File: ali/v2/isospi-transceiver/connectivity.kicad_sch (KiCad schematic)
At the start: 27 parts, among them J7 Conn_01x03, J8 Vertical Ethernet, U3 TJA1462ATK, U4 LAN8742AI, Y2 25 MHz

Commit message: Some BoM Changes, add fabrication toolkit settings
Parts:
- R10, R11, R12, R13: MPN RC0603FR-0747RL -> AC0603FR-0747RL
- R14, R16: MPN RC0603FR-0710KL -> AC0603FR-0710KL
- R17, R18: MPN RC0603FR-07330RL -> AC0603FR-07330RL
- R9: MPN RC0603FR-071K5L -> AC0603FR-071K5L
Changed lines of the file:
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@@
 			)
 		)
-		(property "MPN" "RC0603FR-0747RL"
+		(property "MPN" "AC0603FR-0747RL"
 			(at 100.33 68.58 0)
 			(hide yes)
@@
 			)
 		)
-		(property "MPN" "RC0603FR-0710KL"
+		(property "MPN" "AC0603FR-0710KL"
 			(at 53.34 85.09 90)
 			(hide yes)
@@
 			)
 		)
-		(property "MPN" "RC0603FR-0747RL"
+		(property "MPN" "AC0603FR-0747RL"
 			(at 134.62 68.58 0)
 			(hide yes)
@@
 			)
 		)
-		(property "MPN" "RC0603FR-0747RL"
+		(property "MPN" "AC0603FR-0747RL"
 			(at 111.76 68.58 0)
 			(hide yes)
@@
 			)
 		)
-		(property "MPN" "RC0603FR-07330RL"
+		(property "MPN" "AC0603FR-07330RL"
 			(at 229.87 120.65 0)
 			(hide yes)
@@
 			)
 		)
-		(property "MPN" "RC0603FR-0710KL"
+		(property "MPN" "AC0603FR-0710KL"
 			(at 99.06 102.87 0)
 			(hide yes)
@@
 			)
 		)
-		(property "MPN" "RC0603FR-071K5L"
+		(property "MPN" "AC0603FR-071K5L"
 			(at 43.18 67.31 0)
 			(hide yes)
@@
 			)
 		)
-		(property "MPN" "RC0603FR-07330RL"
+		(property "MPN" "AC0603FR-07330RL"
 			(at 220.98 130.81 0)
 			(hide yes)
@@
 			)
 		)
-		(property "MPN" "RC0603FR-0747RL"
+		(property "MPN" "AC0603FR-0747RL"
 			(at 123.19 68.58 0)
 			(hide yes)

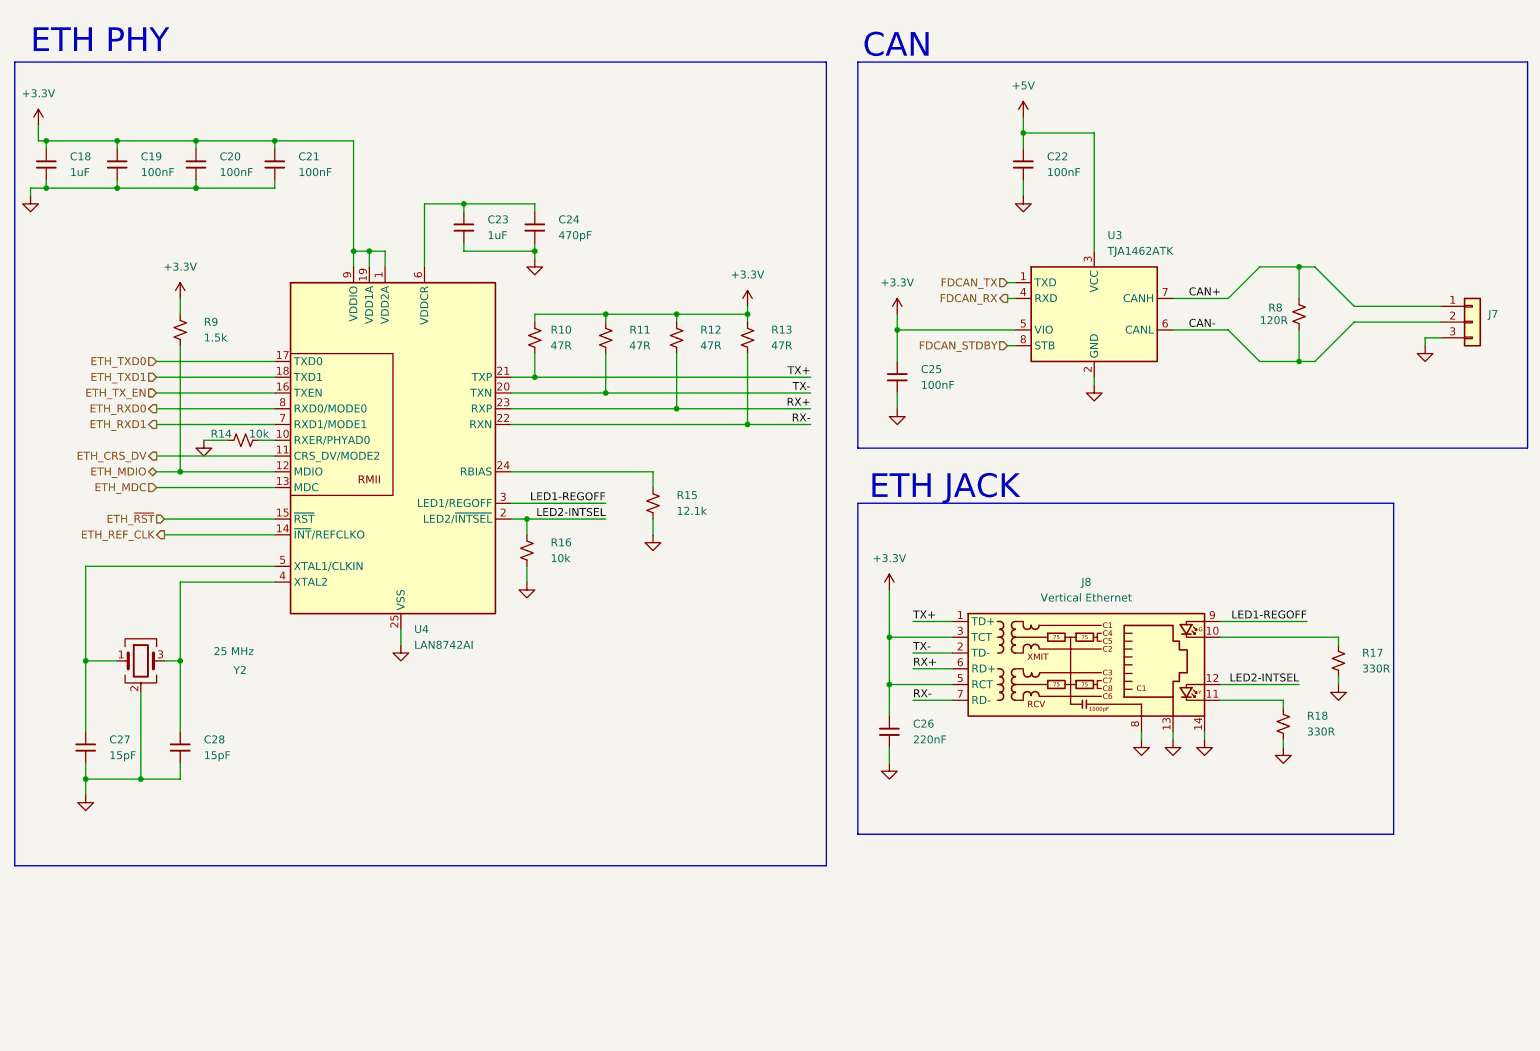
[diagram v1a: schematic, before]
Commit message: Use 1206 on AFEs
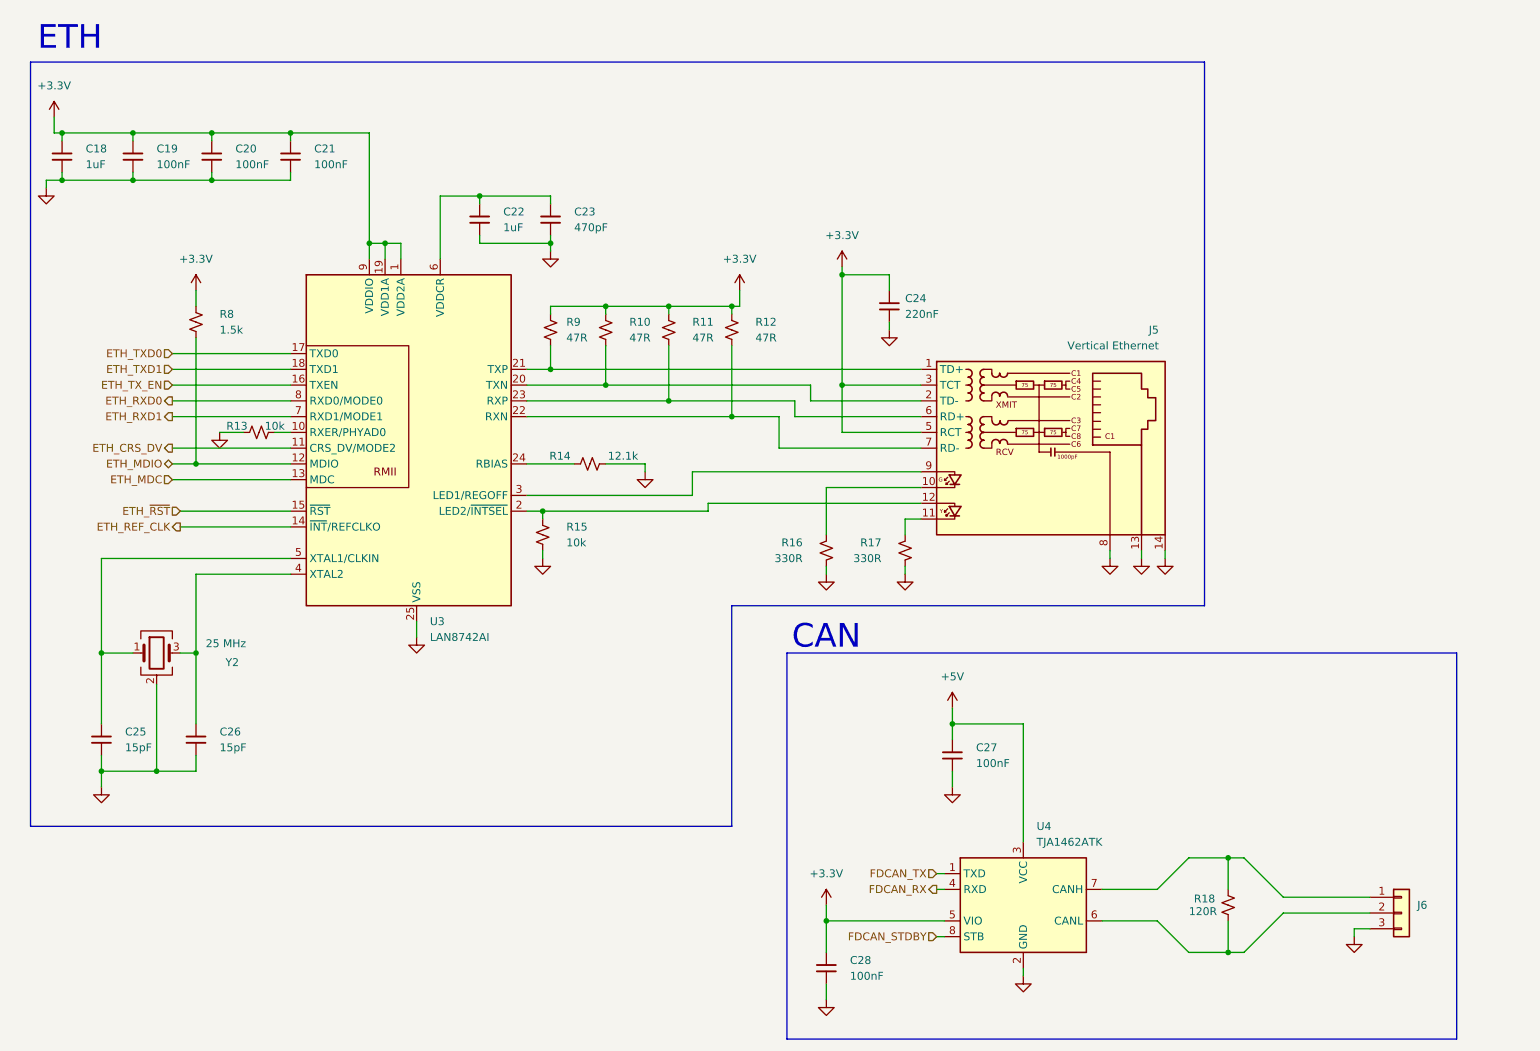
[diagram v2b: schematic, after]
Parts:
- removed J7: Conn_01x03, APRL_Connector_Molex:Molex_CLIK-Mate_503159-0301_1x03-1MP_P1.50mm_Vertical, symbol Connector_Generic:Conn_01x03
- removed J8: Vertical Ethernet, APRL_Connector:RJ45_Hanrun_HY951180A_Vertical, symbol APRL_Connector:RJ45_Hanrun_HY951180A
- removed U3: TJA1462ATK, APRL_Package_QFN:HVSON-8-1EP_3x3mm_P0.65mm_EP1.6x2.4mm_ThermalVias, symbol APRL_Comms:TJA1462ATK
- removed U4: LAN8742AI, APRL_Package_QFN:VQFN-24-1EP_4x4mm_P0.5mm_EP2.5x2.5mm_ThermalVias, symbol APRL_Comms:LAN8742A
- added J5: Vertical Ethernet, APRL_Connector:RJ45_Hanrun_HY951180A_Vertical, symbol APRL_Connector:RJ45_Hanrun_HY951180A
- added J6: Conn_01x03, APRL_Connector_Molex:Molex_CLIK-Mate_503159-0301_1x03-1MP_P1.50mm_Vertical, symbol Connector_Generic:Conn_01x03
- added U3: LAN8742AI, APRL_Package_QFN:VQFN-24-1EP_4x4mm_P0.5mm_EP2.5x2.5mm_ThermalVias, symbol APRL_Comms:LAN8742A
- added U4: TJA1462ATK, APRL_Package_QFN:HVSON-8-1EP_3x3mm_P0.65mm_EP1.6x2.4mm_ThermalVias, symbol APRL_Comms:TJA1462ATK
- C22: value 100nF -> 1uF; MPN GRM188R72A104KA35 -> GRM188D72A105KE01
- C23: value 1uF -> 470pF; MPN GRM188D72A105KE01 -> GRM1885C1H471JA01
- C24: value 470pF -> 220nF; MPN GRM1885C1H471JA01 -> GRM188R71H224KAC4
- C25: value 100nF -> 15pF; MPN GRM188R72A104KA35 -> GRM1885C2E150FW07
- C26: value 220nF -> 15pF; MPN GRM188R71H224KAC4 -> GRM1885C2E150FW07
- C27, C28: value 15pF -> 100nF; MPN GRM1885C2E150FW07 -> GRM188R72A104KA35
- R13: value 47R -> 10k; MPN AC0603FR-0747RL -> AC0603FR-0710KL
- R14: value 10k -> 12.1k; MPN AC0603FR-0710KL -> RT0603BRD0712K1L
- R15: value 12.1k -> 10k; MPN RT0603BRD0712K1L -> AC0603FR-0710KL
- R16: value 10k -> 330R; MPN AC0603FR-0710KL -> AC0603FR-07330RL
- R18: value 330R -> 120R; MPN AC0603FR-07330RL -> AC0603FR-07120RL
- R8: value 120R -> 1.5k; MPN AC0603FR-07120RL -> AC0603FR-071K5L
- R9: value 1.5k -> 47R; MPN AC0603FR-071K5L -> AC0603FR-0747RL
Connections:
- net CAN+ is gone; now on net ETH_MDIO: R8.2
- net CAN- is gone; now on net +3.3V: R8.1
- net +3.3V: now also C24.1, C28.1, J5.3 (TCT), J5.5 (RCT), U3.1 (VDD2A), U3.19 (VDD1A), U3.9 (VDDIO), U4.5 (VIO); no longer C25.1, C26.1, R13.1
- net +5V: now also C27.1, U4.3 (VCC); no longer C22.1
- net ETH_CRS_DV: now also U3.11 (CRS_DV/MODE2)
- net ETH_MDC: now also U3.13 (MDC)
- net ETH_MDIO: now also U3.12 (MDIO); no longer R9.2
- net ETH_REF_CLK: now also U3.14 (~{INT}/REFCLKO)
- net ETH_RXD0: now also U3.8 (RXD0/MODE0)
- net ETH_RXD1: now also U3.7 (RXD1/MODE1)
- net ETH_TXD0: now also U3.17 (TXD0)
- net ETH_TXD1: now also U3.18 (TXD1)
- net ETH_TX_EN: now also U3.16 (TXEN)
- net ETH_~{RST}: now also U3.15 (~{RST})
- net FDCAN_RX: now also U4.4 (RXD)
- net FDCAN_STDBY: now also U4.8 (STB)
- net FDCAN_TX: now also U4.1 (TXD)
- net GND: now also R13.1, R14.2, J5.13, J5.14, J5.8, J6.3 (Pin_3), U3.25 (VSS), U4.2 (GND), U4.9 (GND); no longer R14.1, R18.2
- net at Y2.1: now also C25.1, U3.5 (XTAL1/CLKIN); no longer C27.1
- net at C23.1: now also C22.1, U3.6 (VDDCR); no longer C24.1
- net at R17.1: now also J5.11
- net at R18.1: now also J6.2 (Pin_2), U4.6 (CANL)
- net at R15.1: now also J5.12, U3.2 (LED2/~{INTSEL})
- net at Y2.3: now also C26.1, U3.4 (XTAL2); no longer C28.1
- net LED2-INTSEL: no longer names the net of R16.1
- net LED2-INTSEL: now also J5.10
- net RX+: no longer names the net of R12.2
- net RX+: now also J5.7 (RD-), U3.22 (RXN)
- net RX-: no longer names the net of R13.2
- net RX-: now also U3.10 (RXER/PHYAD0)
- net TX+: no longer names the net of R10.2
- net TX+: now also J5.2 (TD-), U3.20 (TXN)
- net TX-: no longer names the net of R11.2
- net TX-: now also J5.6 (RD+), U3.23 (RXP)
- new net: J6.1 (Pin_1), R18.2, U4.7 (CANH)
- new net: R14.1, U3.24 (RBIAS)
- new net: J5.1 (TD+), R9.2, U3.21 (TXP)
- new net: J5.9, U3.3 (LED1/REGOFF)
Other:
- note added: "ETH"
- note removed: "ETH JACK"
- note removed: "ETH PHY"
